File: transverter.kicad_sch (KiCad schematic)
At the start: 0 parts

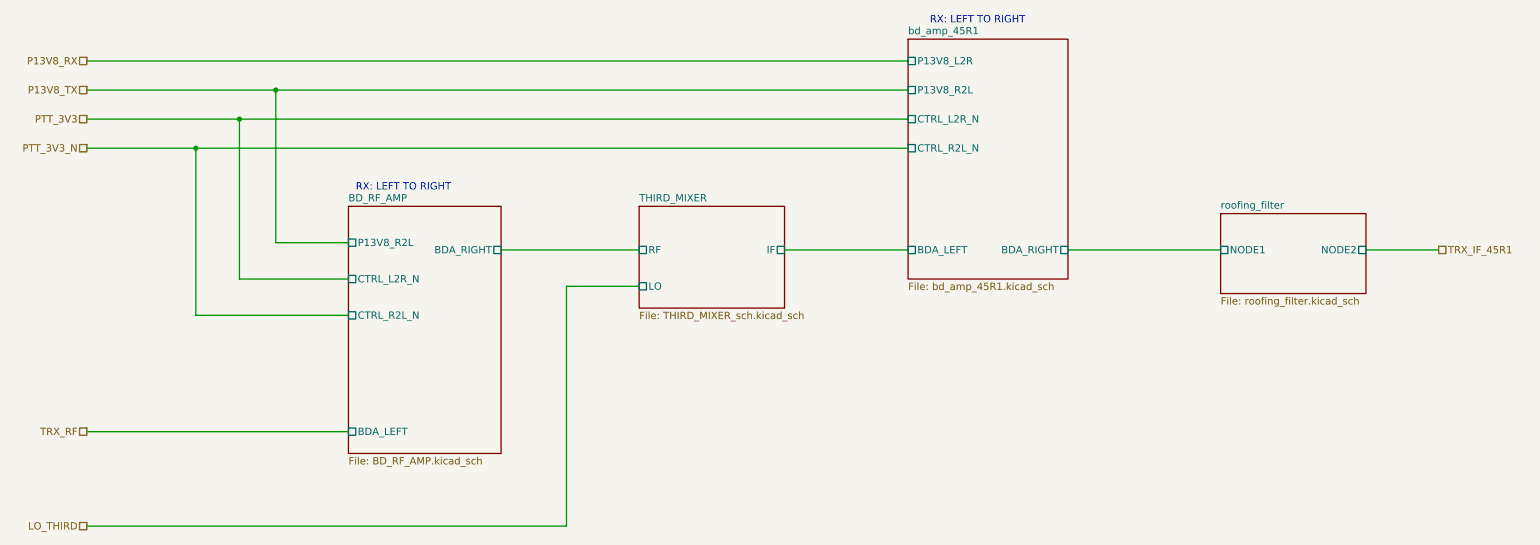
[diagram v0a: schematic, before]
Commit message: trx_mobo_concept_2_B. Change design to use a dedicated 8V supply for the 2SC3357 parts. Add S-Meter connector. Change mic connector to 3 pins and add 8V sopower supply to pin 3.
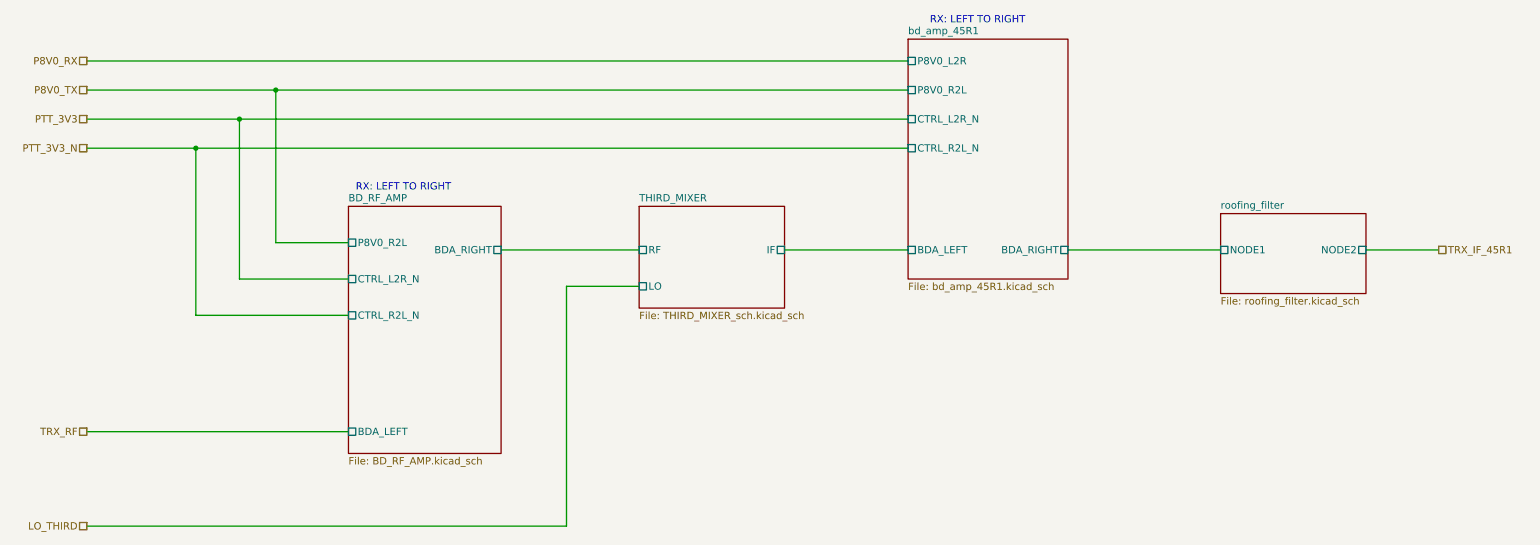
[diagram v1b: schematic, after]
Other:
- sheet BD_RF_AMP ports: added P8V0_R2L; removed P13V8_R2L
- sheet bd_amp_45R1 ports: added P8V0_L2R, P8V0_R2L; removed P13V8_L2R, P13V8_R2L
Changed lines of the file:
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@@
   (paper "A4")
   (title_block
-    (rev "X1")
+    (rev "B")
   )
   (junction (at 63.5 50.8) (diameter 0) (color 0 0 0 0)
@@
     (effects (font (size 1.27 1.27)) (justify left bottom))
   )
-  (hierarchical_label "P13V8_TX" (shape passive) (at 30.48 50.8 180)
+  (hierarchical_label "P8V0_TX" (shape passive) (at 30.48 50.8 180)
     (effects (font (size 1.27 1.27)) (justify right))
   )
@@
     (effects (font (size 1.27 1.27)) (justify right))
   )
-  (hierarchical_label "P13V8_RX" (shape passive) (at 30.48 45.72 180)
+  (hierarchical_label "P8V0_RX" (shape passive) (at 30.48 45.72 180)
     (effects (font (size 1.27 1.27)) (justify right))
   )
@@
       (effects (font (size 1.27 1.27)) (justify right))
     )
-    (pin "P13V8_L2R" passive (at 173.99 45.72 180)
+    (pin "P8V0_L2R" passive (at 173.99 45.72 180)
       (effects (font (size 1.27 1.27)) (justify left))
     )
-    (pin "P13V8_R2L" passive (at 173.99 50.8 180)
+    (pin "P8V0_R2L" passive (at 173.99 50.8 180)
       (effects (font (size 1.27 1.27)) (justify left))
     )
@@
       (effects (font (size 1.27 1.27)) (justify left))
     )
-    (pin "P13V8_R2L" passive (at 76.2 77.47 180)
+    (pin "P8V0_R2L" passive (at 76.2 77.47 180)
       (effects (font (size 1.27 1.27)) (justify left))
     )
